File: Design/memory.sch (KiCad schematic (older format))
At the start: 1 part, among them U3 SST25VF080B-50-4x-S2Ax

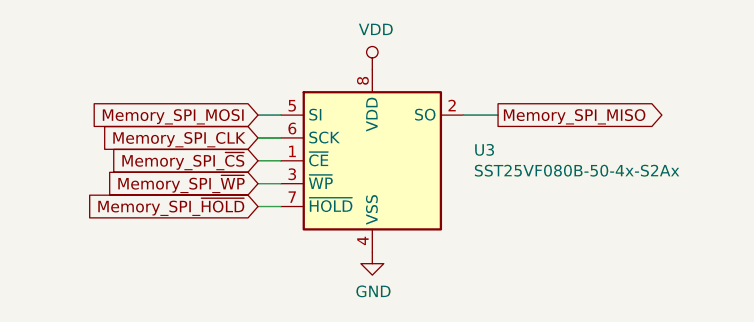
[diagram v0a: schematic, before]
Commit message: Improvement over the Power management: - added TPS6201DRC for raising leaking voltage from supercapacitor - supercap is protected from overvoltage using a shunt diode - power management is using MOSFET logic (2 PFET, 1 NFET)
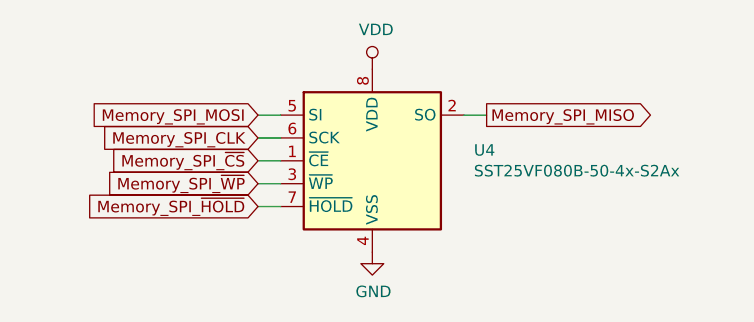
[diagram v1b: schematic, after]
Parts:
- renumbered U3 to U4
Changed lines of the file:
@@
 $EndDescr
 $Comp
-L Memory_Flash:SST25VF080B-50-4x-S2Ax U3
+L Memory_Flash:SST25VF080B-50-4x-S2Ax U4
 U 1 1 5E1DB3D0
 P 2150 1550
-F 0 "U3" H 2594 1596 50  0000 L CNN
+F 0 "U4" H 2594 1596 50  0000 L CNN
 F 1 "SST25VF080B-50-4x-S2Ax" H 2594 1505 50  0000 L CNN
 F 2 "Package_SO:SOIC-8_5.275x5.275mm_P1.27mm" H 2150 850 50  0001 C CNN
@@
 	1650 1350 1750 1350
 $Comp
-L power:VDD #PWR011
+L power:VDD #PWR013
 U 1 1 5E1DDDAD
 P 2150 1150
-F 0 "#PWR011" H 2150 1000 50  0001 C CNN
+F 0 "#PWR013" H 2150 1000 50  0001 C CNN
 F 1 "VDD" H 2167 1323 50  0000 C CNN
 F 2 "" H 2150 1150 50  0001 C CNN
@@
 $EndComp
 $Comp
-L power:GND #PWR012
+L power:GND #PWR014
 U 1 1 5E1E04E0
 P 2150 1950
-F 0 "#PWR012" H 2150 1700 50  0001 C CNN
+F 0 "#PWR014" H 2150 1700 50  0001 C CNN
 F 1 "GND" H 2155 1777 50  0000 C CNN
 F 2 "" H 2150 1950 50  0001 C CNN
@@
 Wire Wire Line
 	1650 1650 1750 1650
-Text GLabel 2700 1350 2    50   Output ~ 0
+Text GLabel 2650 1350 2    50   Output ~ 0
 Memory_SPI_MISO
 Wire Wire Line
-	2700 1350 2550 1350
+	2650 1350 2550 1350
 Text GLabel 1650 1550 0    50   Input ~ 0
 Memory_SPI_~CS~

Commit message: - designed configurable intensity for RGB LEDs - included Breakout (FET, Diode, etc.) Spice models from Cadence Spice - replaced global label with hierarchical complete view - customized net labels with pin function - exported first spice netlist which presents small bugs
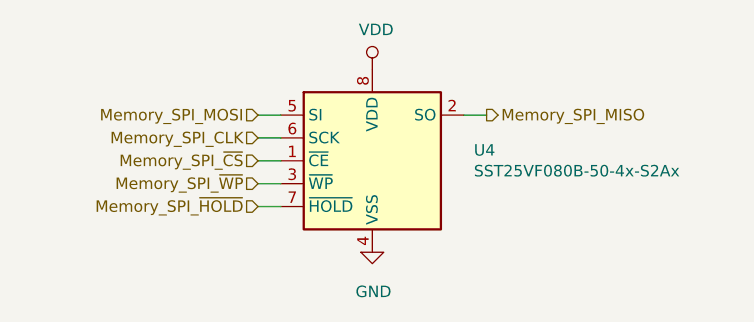
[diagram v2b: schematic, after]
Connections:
- net GND renamed 0
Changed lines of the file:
@@
 $Descr A4 11693 8268
 encoding utf-8
-Sheet 5 7
-Title ""
-Date ""
-Rev ""
-Comp ""
-Comment1 ""
-Comment2 ""
-Comment3 ""
+Sheet 3 6
+Title "meishi_ledger.sch"
+Date "2019-12-13"
+Rev "1.0A"
+Comp "Meishi Smart Luxury"
+Comment1 "Author: Steve Huguenin-Elie"
+Comment2 "Espace de l'Europe"
+Comment3 "2000 Neuchâtel"
 Comment4 ""
 $EndDescr
@@
 	1    0    0    -1
 $EndComp
-Text GLabel 1650 1350 0    50   Input ~ 0
-Memory_SPI_MOSI
-Text GLabel 1650 1450 0    50   Input ~ 0
-Memory_SPI_CLK
 Wire Wire Line
 	1650 1450 1750 1450
@@
 	1650 1350 1750 1350
 $Comp
-L power:VDD #PWR013
+L power:VDD #PWR018
 U 1 1 5E1DDDAD
 P 2150 1150
-F 0 "#PWR013" H 2150 1000 50  0001 C CNN
+F 0 "#PWR018" H 2150 1000 50  0001 C CNN
 F 1 "VDD" H 2167 1323 50  0000 C CNN
 F 2 "" H 2150 1150 50  0001 C CNN
@@
 $EndComp
 $Comp
-L power:GND #PWR014
+L pspice:0 #PWR019
 U 1 1 5E1E04E0
 P 2150 1950
-F 0 "#PWR014" H 2150 1700 50  0001 C CNN
+F 0 "#PWR019" H 2150 1700 50  0001 C CNN
 F 1 "GND" H 2155 1777 50  0000 C CNN
 F 2 "" H 2150 1950 50  0001 C CNN
@@
 	1    0    0    -1
 $EndComp
-Text GLabel 1650 1650 0    50   Input ~ 0
-Memory_SPI_~WP~
-Text GLabel 1650 1750 0    50   Input ~ 0
-Memory_SPI_~HOLD~
 Wire Wire Line
 	1650 1750 1750 1750
 Wire Wire Line
 	1650 1650 1750 1650
-Text GLabel 2650 1350 2    50   Output ~ 0
-Memory_SPI_MISO
 Wire Wire Line
 	2650 1350 2550 1350
-Text GLabel 1650 1550 0    50   Input ~ 0
-Memory_SPI_~CS~
 Wire Wire Line
 	1650 1550 1750 1550
+Text HLabel 1650 1350 0    50   Input ~ 0
+Memory_SPI_MOSI
+Text HLabel 1650 1450 0    50   Input ~ 0
+Memory_SPI_CLK
+Text HLabel 1650 1550 0    50   Input ~ 0
+Memory_SPI_~CS~
+Text HLabel 1650 1650 0    50   Input ~ 0
+Memory_SPI_~WP~
+Text HLabel 1650 1750 0    50   Input ~ 0
+Memory_SPI_~HOLD~
+Text HLabel 2650 1350 2    50   Output ~ 0
+Memory_SPI_MISO
 $EndSCHEMATC
